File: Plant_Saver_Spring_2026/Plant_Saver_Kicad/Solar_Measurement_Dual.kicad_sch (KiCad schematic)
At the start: 13 parts, among them U8 MCP6234

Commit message: Footprint correction
Changed the DHT20 from a header pin to the recommended SIP. Also had to reannotate in order to assign footprints.
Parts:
- renumbered R3 to R10, R4 to R11, R5 to R12, R6 to R13, R11 to R14, R12 to R15, U8 to U13
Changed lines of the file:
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@@
 				)
 				(path "/7f244634-d37a-4ff0-ba36-8027330ab1bd/9d841e6d-e3b2-48a8-9c06-32c643c2cc22"
-					(reference "R49")
+					(reference "R33")
 					(unit 1)
 				)
@@
 		(dnp no)
 		(fields_autoplaced yes)
-		(property "Reference" "R3"
+		(property "Reference" "R10"
 			(at 114.3 64.77 90)
 			(effects
@@
 			(project "Plant_Saver_Kicad"
 				(path "/7f244634-d37a-4ff0-ba36-8027330ab1bd/97049490-2dc1-47ac-bb1c-089fa2bcc51b"
-					(reference "R3")
-					(unit 1)
-				)
-				(path "/7f244634-d37a-4ff0-ba36-8027330ab1bd/9d841e6d-e3b2-48a8-9c06-32c643c2cc22"
-					(reference "R52")
+					(reference "R10")
+					(unit 1)
+				)
+				(path "/7f244634-d37a-4ff0-ba36-8027330ab1bd/9d841e6d-e3b2-48a8-9c06-32c643c2cc22"
+					(reference "R23")
 					(unit 1)
 				)
@@
 		(dnp no)
 		(fields_autoplaced yes)
-		(property "Reference" "R12"
+		(property "Reference" "R15"
 			(at 132.08 100.33 90)
 			(effects
@@
 			(project "Plant_Saver_Kicad"
 				(path "/7f244634-d37a-4ff0-ba36-8027330ab1bd/97049490-2dc1-47ac-bb1c-089fa2bcc51b"
-					(reference "R12")
-					(unit 1)
-				)
-				(path "/7f244634-d37a-4ff0-ba36-8027330ab1bd/9d841e6d-e3b2-48a8-9c06-32c643c2cc22"
-					(reference "R57")
+					(reference "R15")
+					(unit 1)
+				)
+				(path "/7f244634-d37a-4ff0-ba36-8027330ab1bd/9d841e6d-e3b2-48a8-9c06-32c643c2cc22"
+					(reference "R30")
 					(unit 1)
 				)
@@
 				)
 				(path "/7f244634-d37a-4ff0-ba36-8027330ab1bd/9d841e6d-e3b2-48a8-9c06-32c643c2cc22"
-					(reference "R59")
+					(reference "R34")
 					(unit 1)
 				)
@@
 		(dnp no)
 		(fields_autoplaced yes)
-		(property "Reference" "R11"
+		(property "Reference" "R14"
 			(at 132.08 58.42 90)
 			(effects
@@
 			(project "Plant_Saver_Kicad"
 				(path "/7f244634-d37a-4ff0-ba36-8027330ab1bd/97049490-2dc1-47ac-bb1c-089fa2bcc51b"
-					(reference "R11")
-					(unit 1)
-				)
-				(path "/7f244634-d37a-4ff0-ba36-8027330ab1bd/9d841e6d-e3b2-48a8-9c06-32c643c2cc22"
-					(reference "R51")
+					(reference "R14")
+					(unit 1)
+				)
+				(path "/7f244634-d37a-4ff0-ba36-8027330ab1bd/9d841e6d-e3b2-48a8-9c06-32c643c2cc22"
+					(reference "R29")
 					(unit 1)
 				)
@@
 		(on_board yes)
 		(dnp no)
-		(property "Reference" "U8"
+		(property "Reference" "U13"
 			(at 97.79 83.82 90)
 			(effects
@@
 			(project "Plant_Saver_Kicad"
 				(path "/7f244634-d37a-4ff0-ba36-8027330ab1bd/97049490-2dc1-47ac-bb1c-089fa2bcc51b"
-					(reference "U8")
+					(reference "U13")
 					(unit 5)
 				)
 				(path "/7f244634-d37a-4ff0-ba36-8027330ab1bd/9d841e6d-e3b2-48a8-9c06-32c643c2cc22"
-					(reference "U9")
+					(reference "U15")
 					(unit 5)
 				)
@@
 		(on_board yes)
 		(dnp no)
-		(property "Reference" "U8"
+		(property "Reference" "U13"
 			(at 132.08 125.73 0)
 			(effects
@@
 			(project "Plant_Saver_Kicad"
 				(path "/7f244634-d37a-4ff0-ba36-8027330ab1bd/97049490-2dc1-47ac-bb1c-089fa2bcc51b"
-					(reference "U8")
+					(reference "U13")
 					(unit 3)
 				)
 				(path "/7f244634-d37a-4ff0-ba36-8027330ab1bd/9d841e6d-e3b2-48a8-9c06-32c643c2cc22"
-					(reference "U20")
+					(reference "U15")
 					(unit 3)
 				)
@@
 		(dnp no)
 		(fields_autoplaced yes)
-		(property "Reference" "R5"
+		(property "Reference" "R12"
 			(at 120.65 81.2799 0)
 			(effects
@@
 			(project "Plant_Saver_Kicad"
 				(path "/7f244634-d37a-4ff0-ba36-8027330ab1bd/97049490-2dc1-47ac-bb1c-089fa2bcc51b"
-					(reference "R5")
-					(unit 1)
-				)
-				(path "/7f244634-d37a-4ff0-ba36-8027330ab1bd/9d841e6d-e3b2-48a8-9c06-32c643c2cc22"
-					(reference "R50")
+					(reference "R12")
+					(unit 1)
+				)
+				(path "/7f244634-d37a-4ff0-ba36-8027330ab1bd/9d841e6d-e3b2-48a8-9c06-32c643c2cc22"
+					(reference "R25")
 					(unit 1)
 				)
@@
 		(dnp no)
 		(fields_autoplaced yes)
-		(property "Reference" "R6"
+		(property "Reference" "R13"
 			(at 120.65 123.1899 0)
 			(effects
@@
 			(project "Plant_Saver_Kicad"
 				(path "/7f244634-d37a-4ff0-ba36-8027330ab1bd/97049490-2dc1-47ac-bb1c-089fa2bcc51b"
-					(reference "R6")
-					(unit 1)
-				)
-				(path "/7f244634-d37a-4ff0-ba36-8027330ab1bd/9d841e6d-e3b2-48a8-9c06-32c643c2cc22"
-					(reference "R56")
+					(reference "R13")
+					(unit 1)
+				)
+				(path "/7f244634-d37a-4ff0-ba36-8027330ab1bd/9d841e6d-e3b2-48a8-9c06-32c643c2cc22"
+					(reference "R26")
 					(unit 1)
 				)
@@
 				)
 				(path "/7f244634-d37a-4ff0-ba36-8027330ab1bd/9d841e6d-e3b2-48a8-9c06-32c643c2cc22"
-					(reference "R58")
+					(reference "R32")
 					(unit 1)
 				)
@@
 		(on_board yes)
 		(dnp no)
-		(property "Reference" "U8"
+		(property "Reference" "U13"
 			(at 132.08 83.82 0)
 			(effects
@@
 			(project "Plant_Saver_Kicad"
 				(path "/7f244634-d37a-4ff0-ba36-8027330ab1bd/97049490-2dc1-47ac-bb1c-089fa2bcc51b"
-					(reference "U8")
-					(unit 1)
-				)
-				(path "/7f244634-d37a-4ff0-ba36-8027330ab1bd/9d841e6d-e3b2-48a8-9c06-32c643c2cc22"
-					(reference "U9")
+					(reference "U13")
+					(unit 1)
+				)
+				(path "/7f244634-d37a-4ff0-ba36-8027330ab1bd/9d841e6d-e3b2-48a8-9c06-32c643c2cc22"
+					(reference "U15")
 					(unit 1)
 				)
@@
 				)
 				(path "/7f244634-d37a-4ff0-ba36-8027330ab1bd/9d841e6d-e3b2-48a8-9c06-32c643c2cc22"
-					(reference "R53")
+					(reference "R31")
 					(unit 1)
 				)
@@
 				)
 				(path "/7f244634-d37a-4ff0-ba36-8027330ab1bd/9d841e6d-e3b2-48a8-9c06-32c643c2cc22"
-					(reference "R54")
+					(reference "R36")
 					(unit 1)
 				)
@@
 				)
 				(path "/7f244634-d37a-4ff0-ba36-8027330ab1bd/9d841e6d-e3b2-48a8-9c06-32c643c2cc22"
-					(reference "R60")
+					(reference "R37")
 					(unit 1)
 				)
@@
 		(on_board yes)
 		(dnp no)
-		(property "Reference" "U8"
+		(property "Reference" "U13"
 			(at 168.91 86.36 0)
 			(effects
@@
 			(project "Plant_Saver_Kicad"
 				(path "/7f244634-d37a-4ff0-ba36-8027330ab1bd/97049490-2dc1-47ac-bb1c-089fa2bcc51b"
-					(reference "U8")
+					(reference "U13")
 					(unit 2)
 				)
 				(path "/7f244634-d37a-4ff0-ba36-8027330ab1bd/9d841e6d-e3b2-48a8-9c06-32c643c2cc22"
-					(reference "U9")
+					(reference "U15")
 					(unit 2)
 				)
@@
 		(on_board yes)
 		(dnp no)
-		(property "Reference" "U8"
+		(property "Reference" "U13"
 			(at 168.91 128.27 0)
 			(effects
@@
 			(project "Plant_Saver_Kicad"
 				(path "/7f244634-d37a-4ff0-ba36-8027330ab1bd/97049490-2dc1-47ac-bb1c-089fa2bcc51b"
-					(reference "U8")
+					(reference "U13")
 					(unit 4)
 				)
 				(path "/7f244634-d37a-4ff0-ba36-8027330ab1bd/9d841e6d-e3b2-48a8-9c06-32c643c2cc22"
-					(reference "U20")
+					(reference "U15")
 					(unit 4)
 				)
@@
 		(dnp no)
 		(fields_autoplaced yes)
-		(property "Reference" "R4"
+		(property "Reference" "R11"
 			(at 114.3 106.68 90)
 			(effects
@@
 			(project "Plant_Saver_Kicad"
 				(path "/7f244634-d37a-4ff0-ba36-8027330ab1bd/97049490-2dc1-47ac-bb1c-089fa2bcc51b"
-					(reference "R4")
-					(unit 1)
-				)
-				(path "/7f244634-d37a-4ff0-ba36-8027330ab1bd/9d841e6d-e3b2-48a8-9c06-32c643c2cc22"
-					(reference "R55")
-					(unit 1)
-				)
+					(reference "R11")
+					(unit 1)
+				)
+				(path "/7f244634-d37a-4ff0-ba36-8027330ab1bd/9d841e6d-e3b2-48a8-9c06-32c643c2cc22"
+					(reference "R24")
+					(unit 1)
+				)

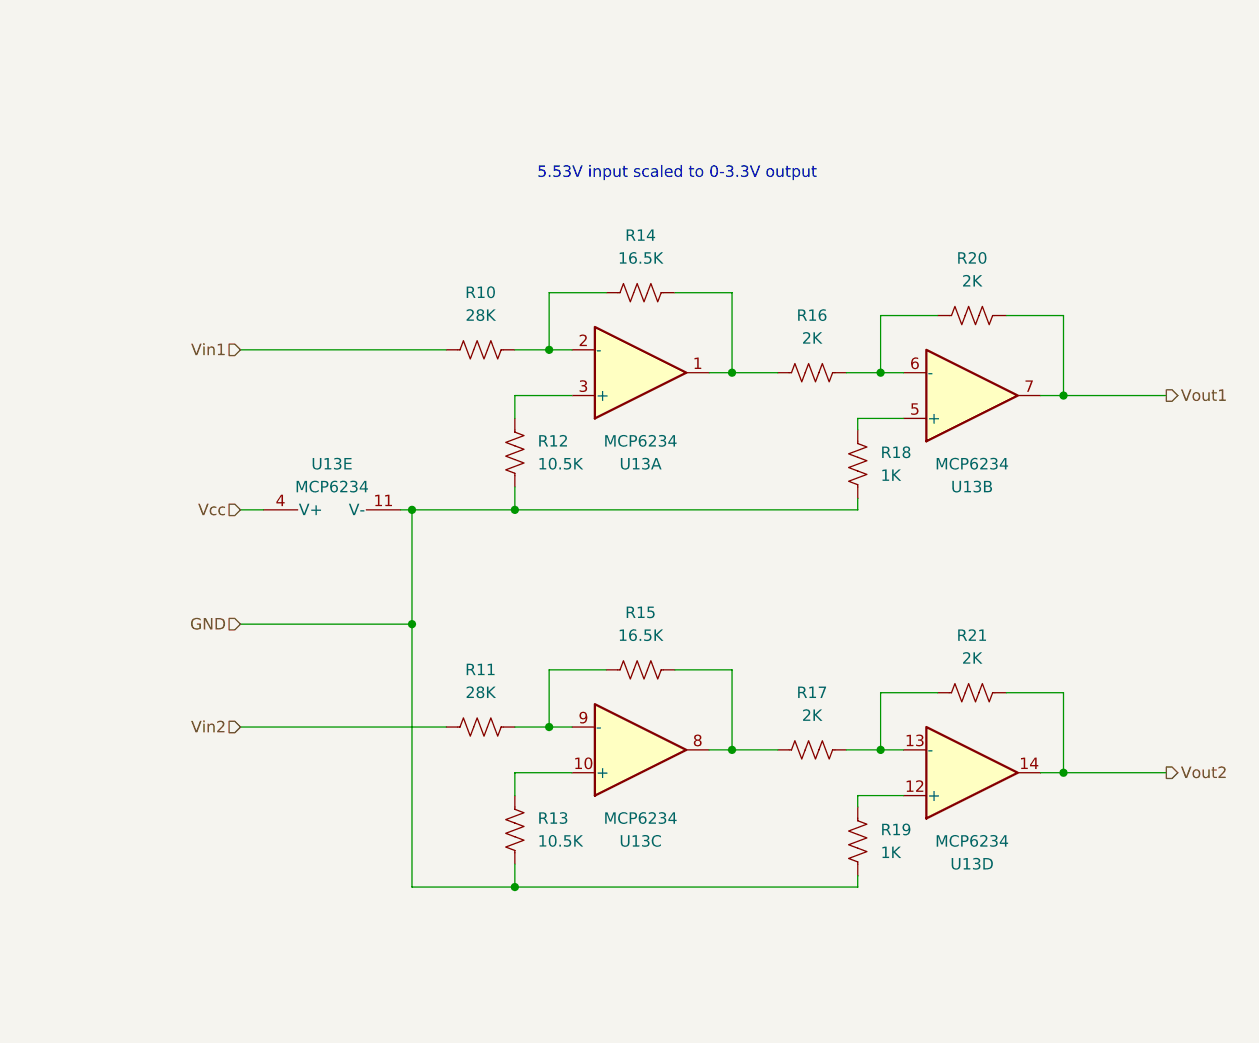
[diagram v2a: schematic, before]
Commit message: Fixed solar measurement circuit
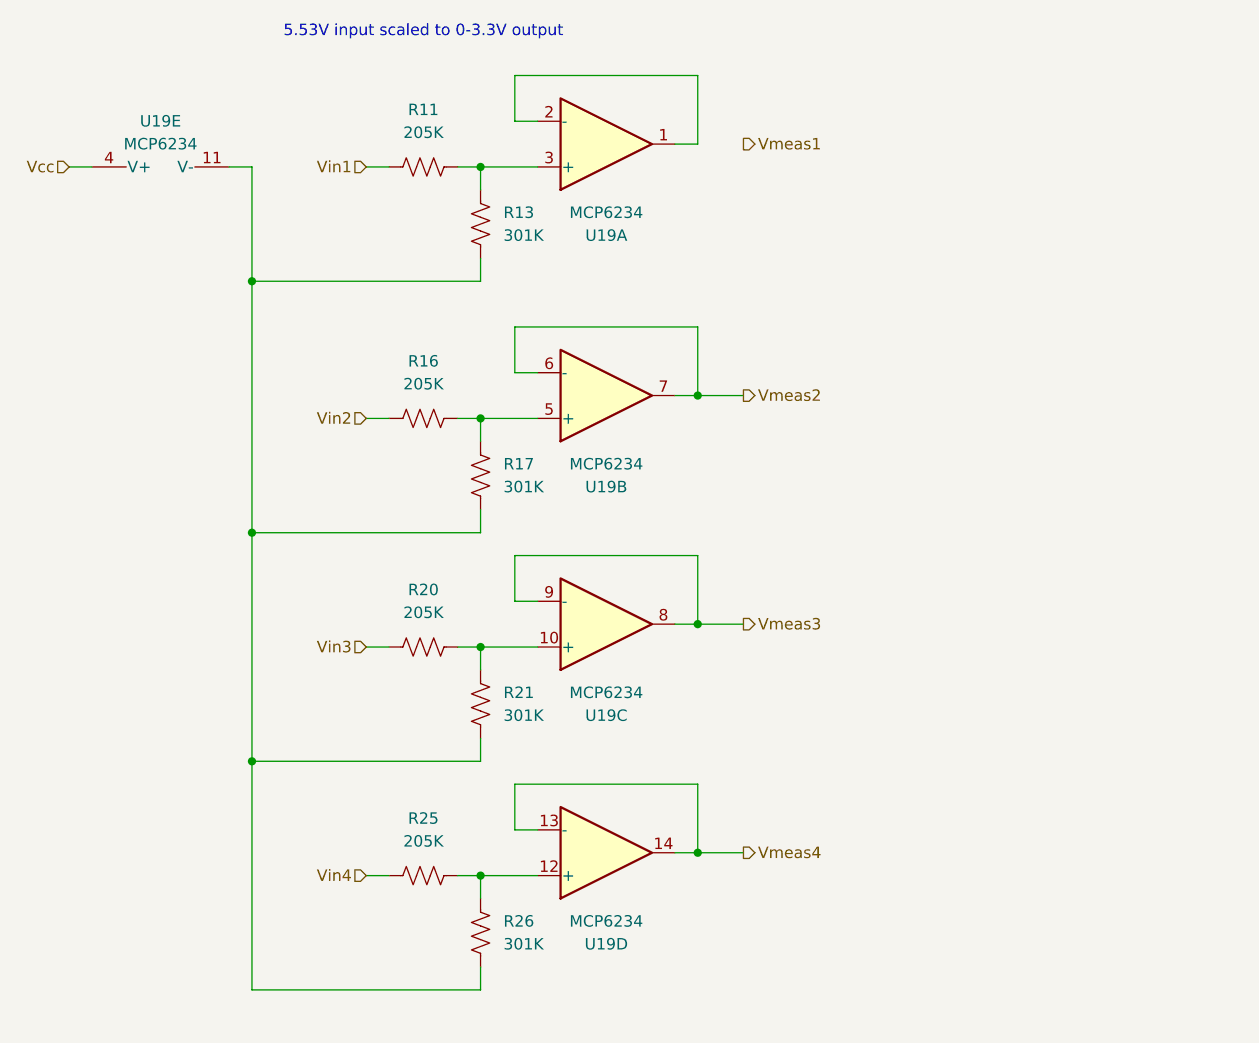
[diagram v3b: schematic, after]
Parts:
- removed R10: 28K, Resistor_THT:R_Axial_DIN0207_L6.3mm_D2.5mm_P10.16mm_Horizontal, symbol Device:R_US
- removed R12: 10.5K, Resistor_THT:R_Axial_DIN0207_L6.3mm_D2.5mm_P10.16mm_Horizontal, symbol Device:R_US
- removed R14, R15: 16.5K, Resistor_THT:R_Axial_DIN0207_L6.3mm_D2.5mm_P10.16mm_Horizontal, symbol Device:R_US
- removed R18, R19: 1K, Resistor_THT:R_Axial_DIN0207_L6.3mm_D2.5mm_P10.16mm_Horizontal, symbol Device:R_US
- removed U13: MCP6234, MCP6234_E_P:PDIP14_300MC_MCH, symbol Amplifier_Operational:OPA1664D
- added R25: 205K, Resistor_THT:R_Axial_DIN0207_L6.3mm_D2.5mm_P10.16mm_Horizontal, symbol Device:R_US
- added R26: 301K, Resistor_THT:R_Axial_DIN0207_L6.3mm_D2.5mm_P10.16mm_Horizontal, symbol Device:R_US
- added U19: MCP6234, MCP6234_E_P:PDIP14_300MC_MCH, symbol Amplifier_Operational:OPA1664D
- R11: value 28K -> 205K
- R13: value 10.5K -> 301K
- R16, R20: value 2K -> 205K
- R17, R21: value 2K -> 301K
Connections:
- net GND is gone; now on an unnamed net: R13.1
- net Vout2 is gone; now on an unnamed net: R21.1
- net Vcc: now also U19.4 (V+)
- net Vin1: now also R11.1
- net Vin2: now also R16.1; no longer R11.2
- net at R17.2: now also R16.2, U19.5 (+)
- net at R13.2: now also R11.2, U19.3 (+)
- net at R17.1: now also R26.1, U19.11 (V-); no longer R21.2
- net at R20.2: now also R21.2, U19.10 (+); no longer R16.1
- net Vout1 renamed Vin3
- new net: R25.2, R26.2, U19.12 (+)
- new net: U19.1, U19.2 (-)
- new net Vin4: R25.1
- new net Vmeas2: U19.6 (-), U19.7
- new net Vmeas3: U19.8, U19.9 (-)
- new net Vmeas4: U19.13 (-), U19.14

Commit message: Added power switching
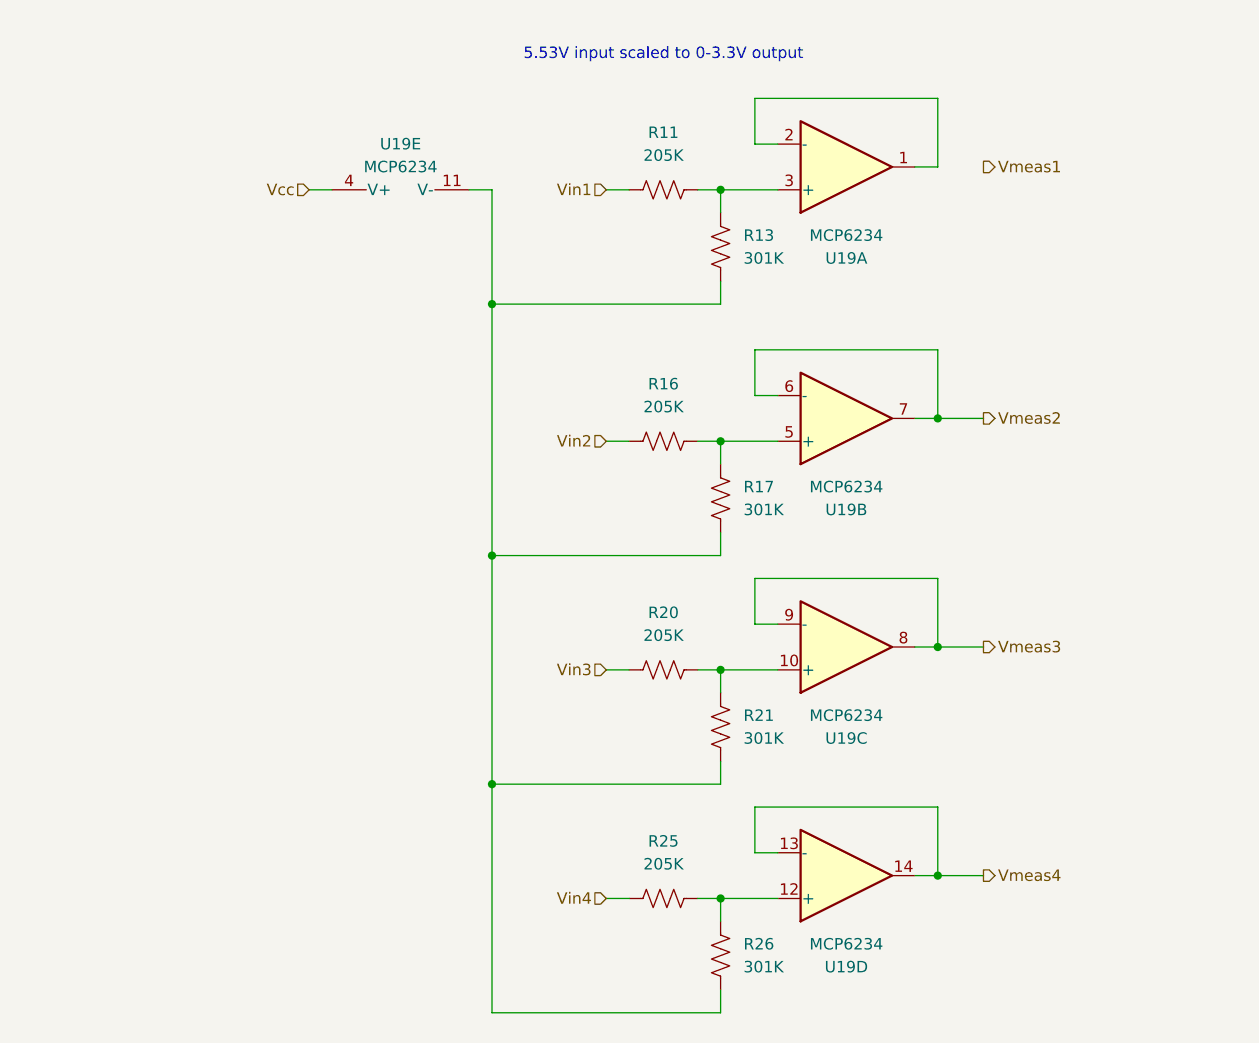
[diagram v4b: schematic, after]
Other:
- moved on the sheet: R11, R13, R16, R17, R20, R21, R25, R26, U19A, U19B, U19C, U19D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

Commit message: Started PCB
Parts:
- renumbered R11 to R28, R16 to R29, R20 to R30, R25 to R31, R13 to R32, R17 to R33, R21 to R34, R26 to R35, U19 to U14
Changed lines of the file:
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@@
 		(dnp no)
 		(fields_autoplaced yes)
-		(property "Reference" "R13"
+		(property "Reference" "R32"
 			(at 143.51 58.4199 0)
 			(effects
@@
 			(project "Plant_Saver_Kicad"
 				(path "/7f244634-d37a-4ff0-ba36-8027330ab1bd/9d841e6d-e3b2-48a8-9c06-32c643c2cc22"
-					(reference "R13")
+					(reference "R32")
 					(unit 1)
 				)
@@
 		(dnp no)
 		(fields_autoplaced yes)
-		(property "Reference" "R17"
+		(property "Reference" "R33"
 			(at 143.51 86.3599 0)
 			(effects
@@
 			(project "Plant_Saver_Kicad"
 				(path "/7f244634-d37a-4ff0-ba36-8027330ab1bd/9d841e6d-e3b2-48a8-9c06-32c643c2cc22"
-					(reference "R17")
+					(reference "R33")
 					(unit 1)
 				)
@@
 		(on_board yes)
 		(dnp no)
-		(property "Reference" "U19"
+		(property "Reference" "U14"
 			(at 154.94 88.9 0)
 			(effects
@@
 			(project "Plant_Saver_Kicad"
 				(path "/7f244634-d37a-4ff0-ba36-8027330ab1bd/9d841e6d-e3b2-48a8-9c06-32c643c2cc22"
-					(reference "U19")
+					(reference "U14")
 					(unit 2)
 				)
@@
 		(on_board yes)
 		(dnp no)
-		(property "Reference" "U19"
+		(property "Reference" "U14"
 			(at 154.94 139.7 0)
 			(effects
@@
 			(project "Plant_Saver_Kicad"
 				(path "/7f244634-d37a-4ff0-ba36-8027330ab1bd/9d841e6d-e3b2-48a8-9c06-32c643c2cc22"
-					(reference "U19")
+					(reference "U14")
 					(unit 4)
 				)
@@
 		(on_board yes)
 		(dnp no)
-		(property "Reference" "U19"
+		(property "Reference" "U14"
 			(at 154.94 114.3 0)
 			(effects
@@
 			(project "Plant_Saver_Kicad"
 				(path "/7f244634-d37a-4ff0-ba36-8027330ab1bd/9d841e6d-e3b2-48a8-9c06-32c643c2cc22"
-					(reference "U19")
+					(reference "U14")
 					(unit 3)
 				)
@@
 		(dnp no)
 		(fields_autoplaced yes)
-		(property "Reference" "R21"
+		(property "Reference" "R34"
 			(at 143.51 111.7599 0)
 			(effects
@@
 			(project "Plant_Saver_Kicad"
 				(path "/7f244634-d37a-4ff0-ba36-8027330ab1bd/9d841e6d-e3b2-48a8-9c06-32c643c2cc22"
-					(reference "R21")
+					(reference "R34")
 					(unit 1)
 				)
@@
 		(dnp no)
 		(fields_autoplaced yes)
-		(property "Reference" "R26"
+		(property "Reference" "R35"
 			(at 143.51 137.1599 0)
 			(effects
@@
 			(project "Plant_Saver_Kicad"
 				(path "/7f244634-d37a-4ff0-ba36-8027330ab1bd/9d841e6d-e3b2-48a8-9c06-32c643c2cc22"
-					(reference "R26")
+					(reference "R35")
 					(unit 1)
 				)
@@
 		(on_board yes)
 		(dnp no)
-		(property "Reference" "U19"
+		(property "Reference" "U14"
 			(at 105.41 48.26 90)
 			(effects
@@
 			(project "Plant_Saver_Kicad"
 				(path "/7f244634-d37a-4ff0-ba36-8027330ab1bd/9d841e6d-e3b2-48a8-9c06-32c643c2cc22"
-					(reference "U19")
+					(reference "U14")
 					(unit 5)
 				)
@@
 		(dnp no)
 		(fields_autoplaced yes)
-		(property "Reference" "R11"
+		(property "Reference" "R28"
 			(at 134.62 46.99 90)
 			(effects
@@
 			(project "Plant_Saver_Kicad"
 				(path "/7f244634-d37a-4ff0-ba36-8027330ab1bd/9d841e6d-e3b2-48a8-9c06-32c643c2cc22"
-					(reference "R11")
+					(reference "R28")
 					(unit 1)
 				)
@@
 		(dnp no)
 		(fields_autoplaced yes)
-		(property "Reference" "R25"
+		(property "Reference" "R31"
 			(at 134.62 125.73 90)
 			(effects
@@
 			(project "Plant_Saver_Kicad"
 				(path "/7f244634-d37a-4ff0-ba36-8027330ab1bd/9d841e6d-e3b2-48a8-9c06-32c643c2cc22"
-					(reference "R25")
+					(reference "R31")
 					(unit 1)
 				)
@@
 		(dnp no)
 		(fields_autoplaced yes)
-		(property "Reference" "R16"
+		(property "Reference" "R29"
 			(at 134.62 74.93 90)
 			(effects
@@
 			(project "Plant_Saver_Kicad"
 				(path "/7f244634-d37a-4ff0-ba36-8027330ab1bd/9d841e6d-e3b2-48a8-9c06-32c643c2cc22"
-					(reference "R16")
+					(reference "R29")
 					(unit 1)
 				)
@@
 		(on_board yes)
 		(dnp no)
-		(property "Reference" "U19"
+		(property "Reference" "U14"
 			(at 154.94 60.96 0)
 			(effects
@@
 			(project "Plant_Saver_Kicad"
 				(path "/7f244634-d37a-4ff0-ba36-8027330ab1bd/9d841e6d-e3b2-48a8-9c06-32c643c2cc22"
-					(reference "U19")
+					(reference "U14")
 					(unit 1)
 				)
@@
 		(dnp no)
 		(fields_autoplaced yes)
-		(property "Reference" "R20"
+		(property "Reference" "R30"
 			(at 134.62 100.33 90)
 			(effects
@@
 			(project "Plant_Saver_Kicad"
 				(path "/7f244634-d37a-4ff0-ba36-8027330ab1bd/9d841e6d-e3b2-48a8-9c06-32c643c2cc22"
-					(reference "R20")
+					(reference "R30")
 					(unit 1)
 				)
